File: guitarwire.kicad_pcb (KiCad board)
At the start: 2 copper layers, 26 x 65 mm, 9 parts, among them J1 JACK_OUT

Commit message: Export gerbers.
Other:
- board text added: "DATE 2025-11-15"
- board text removed: "DATE $Date"
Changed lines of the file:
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@@
 			(outputformat 1)
 			(mirror no)
-			(drillshape 1)
+			(drillshape 0)
 			(scaleselection 1)
-			(outputdirectory "")
+			(outputdirectory "gerbers/")
 		)
 	)
@@
 		)
 	)
-	(gr_text "DATE $Date"
+	(gr_text "DATE 2025-11-15"
 		(at 81 73.25 270)
 		(layer "B.SilkS")

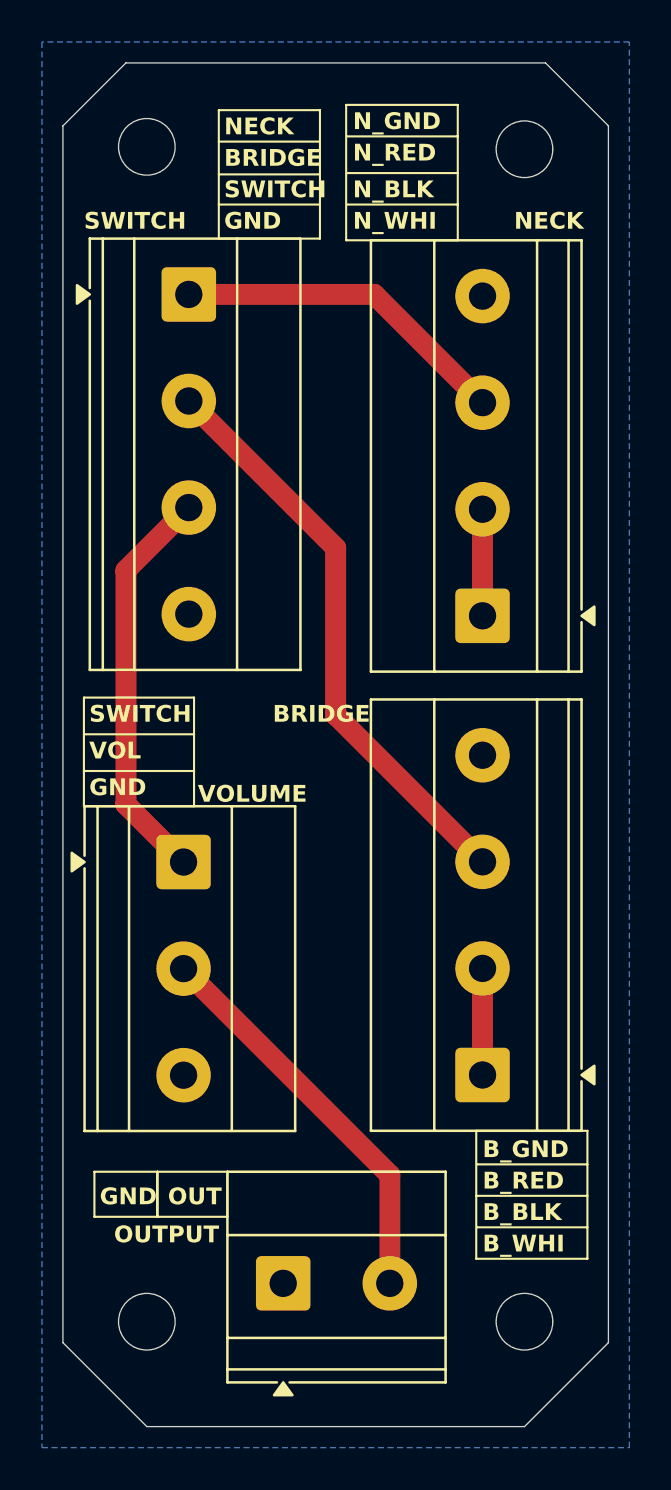
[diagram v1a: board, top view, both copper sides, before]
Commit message: Redesign board to use JST XH connectors.
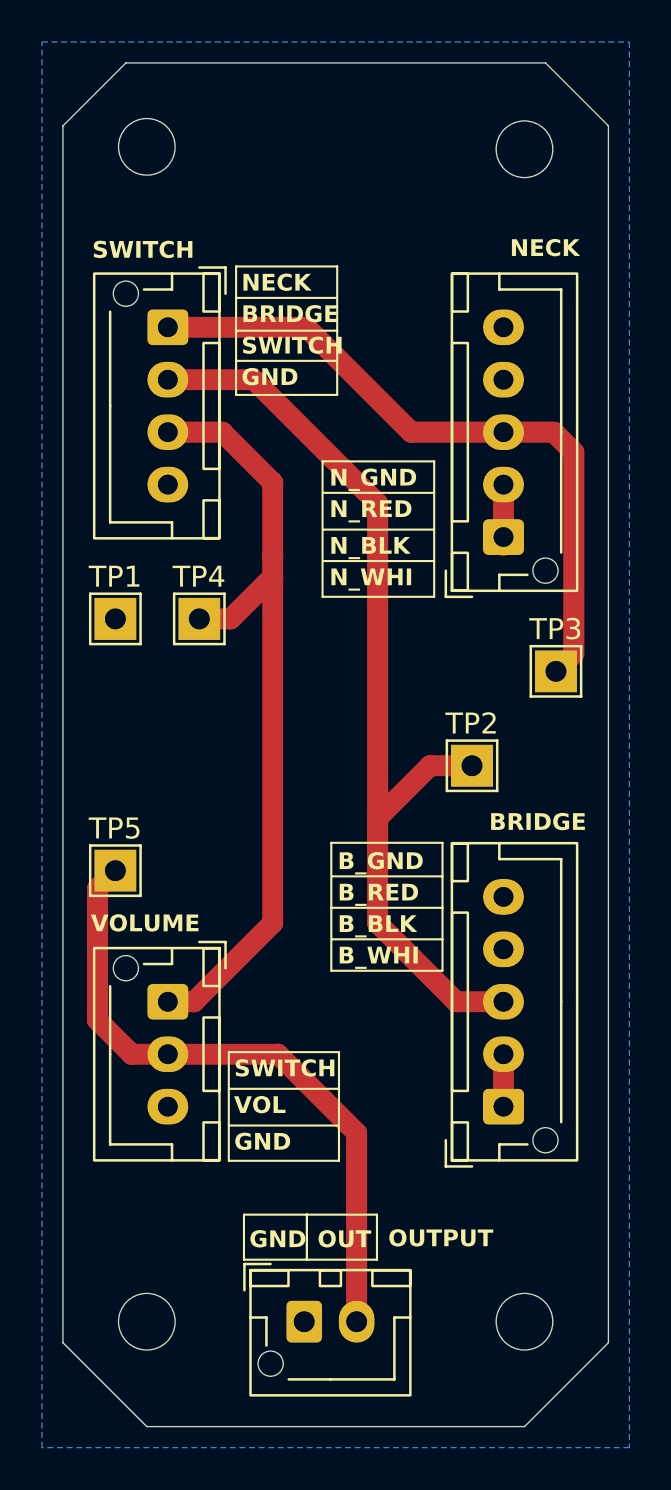
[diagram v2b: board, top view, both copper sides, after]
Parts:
- added TP1: TestPoint, TestPoint:TestPoint_THTPad_2.0x2.0mm_Drill1.0mm, F.Cu at (72.5, 56.5)
- added TP2: TestPoint, TestPoint:TestPoint_THTPad_2.0x2.0mm_Drill1.0mm, F.Cu at (89.5, 63.5)
- added TP3: TestPoint, TestPoint:TestPoint_THTPad_2.0x2.0mm_Drill1.0mm, F.Cu at (93.5, 59.0)
- added TP4: TestPoint, TestPoint:TestPoint_THTPad_2.0x2.0mm_Drill1.0mm, F.Cu at (76.5, 56.5)
- added TP5: TestPoint, TestPoint:TestPoint_THTPad_2.0x2.0mm_Drill1.0mm, F.Cu at (72.5, 68.5)
- HB_BRIDGE1, HB_NECK1: footprint TerminalBlock_Phoenix:TerminalBlock_Phoenix_MKDS-1,5-4-5.08_1x04_P5.08mm_Horizontal -> Connector_JST:JST_XH_B5B-XH-AM_1x05_P2.50mm_Vertical
- J1: footprint TerminalBlock_Phoenix:TerminalBlock_Phoenix_MKDS-1,5-2-5.08_1x02_P5.08mm_Horizontal -> Connector_JST:JST_XH_B2B-XH-AM_1x02_P2.50mm_Vertical
- PICKUP_SELECTOR1: footprint TerminalBlock_Phoenix:TerminalBlock_Phoenix_MKDS-1,5-4-5.08_1x04_P5.08mm_Horizontal -> Connector_JST:JST_XH_B4B-XH-AM_1x04_P2.50mm_Vertical
- VOLUME1: footprint TerminalBlock_Phoenix:TerminalBlock_Phoenix_MKDS-1,5-3-5.08_1x03_P5.08mm_Horizontal -> Connector_JST:JST_XH_B3B-XH-AM_1x03_P2.50mm_Vertical
- moved VOLUME1 6.70 mm to (75.0, 74.8)
- moved HB_NECK1 3.88 mm to (91.0, 52.6)
- moved J1 2.08 mm to (81.5, 90.0)
- moved PICKUP_SELECTOR1 1.86 mm to (75.0, 42.6)
- moved HB_BRIDGE1 1.81 mm to (91.0, 79.8)
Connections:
- net /BRIDGE_INPUT renamed IN_BRIDGE
- net /NECK_INPUT renamed IN_NECK
- net /NECK_MERGE renamed Net-(HB_NECK1-HB_BLACK)
- net /SWITCH_OUT renamed OUT_SWITCH
- net /VOLUME_OUT renamed OUTPUT
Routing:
- net IN_BRIDGE: track 27.8 -> 47.0 mm
- net OUT_SWITCH: track 19.3 -> 37.9 mm
- net IN_NECK: track 16.1 -> 32.6 mm
- net OUTPUT: track 19.1 -> 31.1 mm
- net Net-(HB_NECK1-HB_BLACK): track 5.08 -> 2.50 mm
- net /BRIDGE_MERGE: track 5.08 -> 2.50 mm
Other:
- board text added: "DATE 2026-02-02"
- board text added: "VERSION 2.0.0"
- board text removed: "DATE 2025-11-15"
- board text removed: "VERSION 1.0.0"
